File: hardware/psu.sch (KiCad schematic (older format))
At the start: 17 parts

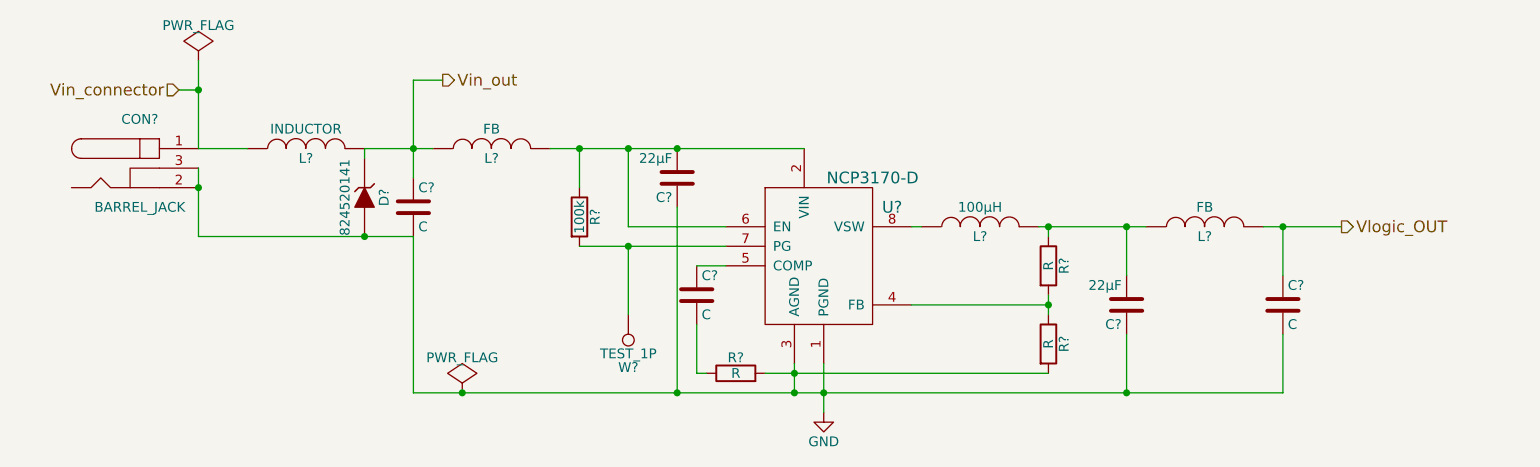
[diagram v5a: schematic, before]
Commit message: Added initial CPU block and fixed bugs from other sheets
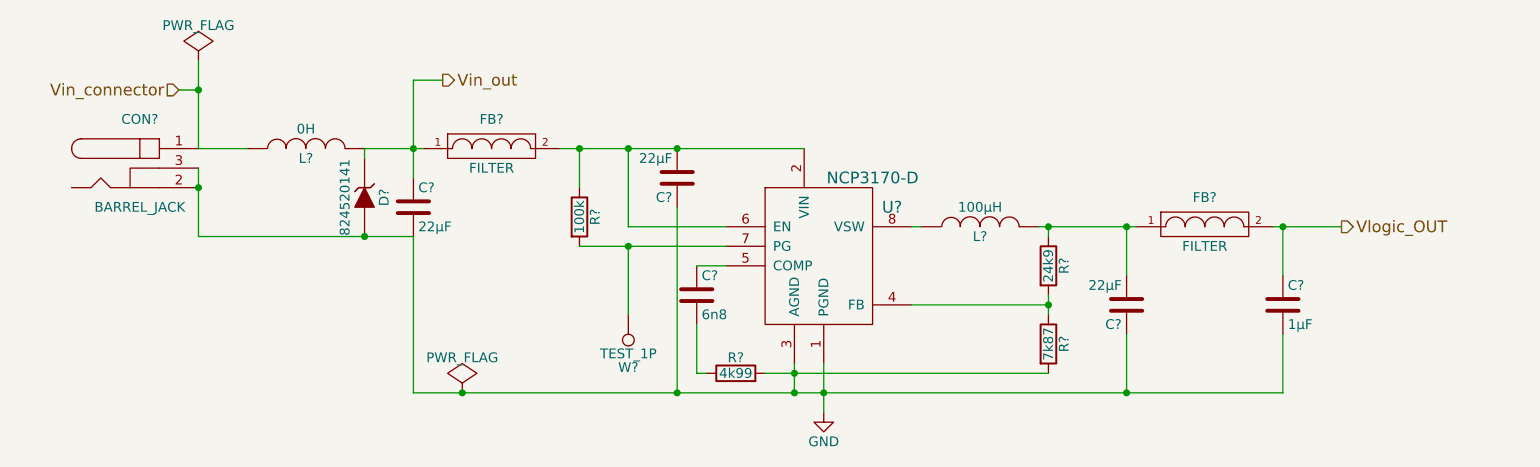
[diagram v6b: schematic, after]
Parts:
- removed L? (x2): FB, symbol INDUCTOR
- added FB? (x2): FILTER, symbol FILTER
- C?: value C -> 6n8
- C?: value C -> 22µF
- C?: value C -> 1µF
- L?: value INDUCTOR -> 0H
- R?: value R -> 24k9
- R?: value R -> 7k87
- R?: value R -> 4k99
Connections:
- net Vin_out: now also FB?.1
- net Vlogic_OUT: now also FB?.2
- net at C?.2, R?.1, U?.2 (VIN)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: now also FB?.2
- net at C?.2, L?.2, R?.1: now also FB?.1
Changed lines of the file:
@@
 LIBS:dodekaedri
 LIBS:Oscillators
+LIBS:stm32
 LIBS:dodekaedri-cache
 EELAYER 25 0
@@
 $Descr A4 11693 8268
 encoding utf-8
-Sheet 4 7
+Sheet 4 8
 Title "Power supply unit"
 Date "2016-09-22"
-Rev "0.1"
+Rev "0.4"
 Comp "PRK - OH2TI"
 Comment1 "exla - OH2EHK"
@@
 P 4800 3700
 F 0 "C?" H 4825 3800 50  0000 L CNN
-F 1 "C" H 4825 3600 50  0000 L CNN
+F 1 "6n8" H 4825 3600 50  0000 L CNN
 F 2 "" H 4838 3550 50  0000 C CNN
 F 3 "" H 4800 3700 50  0000 C CNN
@@
 P 6600 3550
 F 0 "R?" V 6680 3550 50  0000 C CNN
-F 1 "R" V 6600 3550 50  0000 C CNN
+F 1 "24k9" V 6600 3550 50  0000 C CNN
 F 2 "" V 6530 3550 50  0000 C CNN
 F 3 "" H 6600 3550 50  0000 C CNN
@@
 P 6600 3950
 F 0 "R?" V 6680 3950 50  0000 C CNN
-F 1 "R" V 6600 3950 50  0000 C CNN
+F 1 "7k87" V 6600 3950 50  0000 C CNN
 F 2 "" V 6530 3950 50  0000 C CNN
 F 3 "" H 6600 3950 50  0000 C CNN
@@
 P 5000 4100
 F 0 "R?" V 5080 4100 50  0000 C CNN
-F 1 "R" V 5000 4100 50  0000 C CNN
+F 1 "4k99" V 5000 4100 50  0000 C CNN
 F 2 "" V 4930 4100 50  0000 C CNN
 F 3 "" H 5000 4100 50  0000 C CNN
@@
 Wire Wire Line
 	6600 3400 6600 3350
-Wire Wire Line
-	6550 3350 7100 3350
 Wire Wire Line
 	6600 3700 6600 3800
@@
 P 3350 3250
 F 0 "C?" H 3375 3350 50  0000 L CNN
-F 1 "C" H 3375 3150 50  0000 L CNN
+F 1 "22µF" H 3375 3150 50  0000 L CNN
 F 2 "" H 3388 3100 50  0000 C CNN
 F 3 "" H 3350 3250 50  0000 C CNN
@@
 Wire Wire Line
 	2250 3400 3350 3400
-$Comp
-L INDUCTOR L?
-U 1 1 57E32B5E
-P 3750 2950
-F 0 "L?" V 3700 2950 50  0000 C CNN
-F 1 "FB" V 3850 2950 50  0000 C CNN
-F 2 "" H 3750 2950 50  0000 C CNN
-F 3 "" H 3750 2950 50  0000 C CNN
-	1    3750 2950
-	0    -1   -1   0
-$EndComp
-Wire Wire Line
-	4050 2950 5350 2950
+Wire Wire Line
+	4100 2950 5350 2950
 Wire Wire Line
 	4700 3250 4700 4200
 Connection ~ 4700 4200
-$Comp
-L INDUCTOR L?
-U 1 1 57E32E6B
-P 7400 3350
-F 0 "L?" V 7350 3350 50  0000 C CNN
-F 1 "FB" V 7500 3350 50  0000 C CNN
-F 2 "" H 7400 3350 50  0000 C CNN
-F 3 "" H 7400 3350 50  0000 C CNN
-	1    7400 3350
-	0    -1   -1   0
-$EndComp
 $Comp
 L C C?
@@
 P 7800 3750
 F 0 "C?" H 7825 3850 50  0000 L CNN
-F 1 "C" H 7825 3650 50  0000 L CNN
+F 1 "1µF" H 7825 3650 50  0000 L CNN
 F 2 "" H 7838 3600 50  0000 C CNN
 F 3 "" H 7800 3750 50  0000 C CNN
@@
 	1    0    0    -1
 $EndComp
-Wire Wire Line
-	7700 3350 8100 3350
 Connection ~ 7800 3350
 Wire Wire Line
@@
 P 2800 2950
 F 0 "L?" V 2750 2950 50  0000 C CNN
-F 1 "INDUCTOR" V 2900 2950 50  0000 C CNN
+F 1 "0H" V 2900 2950 50  0000 C CNN
 F 2 "" H 2800 2950 50  0000 C CNN
 F 3 "" H 2800 2950 50  0000 C CNN
@@
 $EndComp
 Wire Wire Line
-	3100 2950 3450 2950
+	3100 2950 3400 2950
 Connection ~ 2250 2650
 Wire Wire Line
@@
 Wire Wire Line
 	3500 2600 3350 2600
+$Comp
+L FILTER FB?
+U 1 1 57E5F407
+P 3750 2950
+F 0 "FB?" H 3750 3100 50  0000 C CNN
+F 1 "FILTER" H 3750 2850 50  0000 C CNN
+F 2 "" H 3750 2950 50  0000 C CNN
+F 3 "" H 3750 2950 50  0000 C CNN
+	1    3750 2950
+	1    0    0    -1
+$EndComp
+$Comp
+L FILTER FB?
+U 1 1 57E5F6B8
+P 7400 3350
+F 0 "FB?" H 7400 3500 50  0000 C CNN
+F 1 "FILTER" H 7400 3250 50  0000 C CNN
+F 2 "" H 7400 3350 50  0000 C CNN
+F 3 "" H 7400 3350 50  0000 C CNN
+	1    7400 3350
+	1    0    0    -1
+$EndComp
+Wire Wire Line
+	7750 3350 8100 3350
+Wire Wire Line
+	6550 3350 7050 3350
 $EndSCHEMATC

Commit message: Made some minor adjustments and replotted schematic .pdf
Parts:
- added D?: MSP3V3, symbol ZENER
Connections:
- net GND: now also C?.2, D?.2 (A); no longer C?.1
- net Vlogic_OUT: now also D?.1 (K)
- net at FB?.1, L?.2, R?.1: now also C?.1; no longer C?.2
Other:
- moved on the sheet: C?
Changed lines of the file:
@@
 F 3 "" H 7000 3750 50  0000 C CNN
 	1    7000 3750
-	-1   0    0    1
+	1    0    0    -1
 $EndComp
 $Comp
@@
 	5450 4050 5450 4300
 Wire Wire Line
-	3350 4200 7800 4200
-Wire Wire Line
-	7000 3900 7000 4200
+	3350 4200 8150 4200
 Wire Wire Line
 	7000 3350 7000 3600
@@
 	4950 3350 4450 3350
 Wire Wire Line
-	4450 3350 4450 2950
+	4450 2950 4450 3350
 Connection ~ 4700 2950
 Wire Wire Line
@@
 Connection ~ 4450 2950
 Wire Wire Line
-	2250 3050 2250 3400
+	2250 3050 2250 3450
 Connection ~ 5300 4200
 Connection ~ 2250 3150
@@
 L C C?
 U 1 1 57E32ACD
-P 3350 3250
-F 0 "C?" H 3375 3350 50  0000 L CNN
-F 1 "22µF" H 3375 3150 50  0000 L CNN
-F 2 "" H 3388 3100 50  0000 C CNN
-F 3 "" H 3350 3250 50  0000 C CNN
-	1    3350 3250
-	1    0    0    -1
-$EndComp
-Wire Wire Line
-	2250 3400 3350 3400
+P 3350 3200
+F 0 "C?" H 3375 3300 50  0000 L CNN
+F 1 "22µF" H 3375 3100 50  0000 L CNN
+F 2 "" H 3388 3050 50  0000 C CNN
+F 3 "" H 3350 3200 50  0000 C CNN
+	1    3350 3200
+	1    0    0    -1
+$EndComp
 Wire Wire Line
 	4100 2950 5350 2950
@@
 Wire Wire Line
 	7800 3350 7800 3600
-Text HLabel 8100 3350 2    60   Output ~ 0
+Text HLabel 8350 3350 2    60   Output ~ 0
 Vlogic_OUT
 $Comp
@@
 Connection ~ 2250 2650
 Wire Wire Line
-	3350 2600 3350 3100
+	3350 2600 3350 3050
 $Comp
 L ZENER D?
@@
 	0    1    1    0
 $EndComp
-Connection ~ 3100 3400
-Wire Wire Line
-	3100 3000 3100 2950
+Connection ~ 3100 3450
 Wire Wire Line
 	2250 2950 2500 2950
 Wire Wire Line
-	3350 3400 3350 4200
+	3350 3350 3350 4200
 Text HLabel 3500 2600 2    60   Output ~ 0
 Vin_out
@@
 $EndComp
 Wire Wire Line
-	7750 3350 8100 3350
+	7750 3350 8350 3350
 Wire Wire Line
 	6550 3350 7050 3350
+$Comp
+L ZENER D?
+U 1 1 57ED7CD8
+P 8150 3750
+F 0 "D?" H 8150 3850 50  0000 C CNN
+F 1 "MSP3V3" H 8150 3650 50  0000 C CNN
+F 2 "" H 8150 3750 50  0000 C CNN
+F 3 "" H 8150 3750 50  0000 C CNN
+	1    8150 3750
+	0    1    1    0
+$EndComp
+Wire Wire Line
+	8150 3550 8150 3350
+Connection ~ 8150 3350
+Wire Wire Line
+	8150 4200 8150 3950
+Connection ~ 7800 4200
+Connection ~ 3350 3450
+Wire Wire Line
+	3100 3000 3100 2950
+Wire Wire Line
+	2250 3450 3350 3450
+Wire Wire Line
+	3100 3400 3100 3450
+Wire Wire Line
+	7000 3900 7000 4200
 $EndSCHEMATC

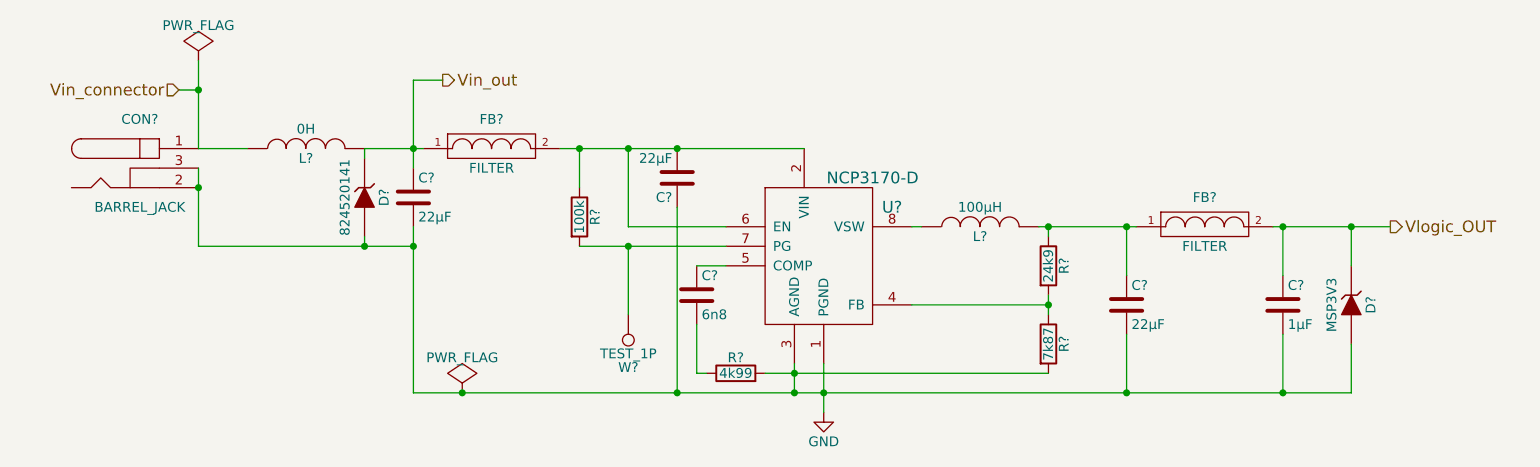
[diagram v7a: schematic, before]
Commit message: Fixed 8/11 of issue #4
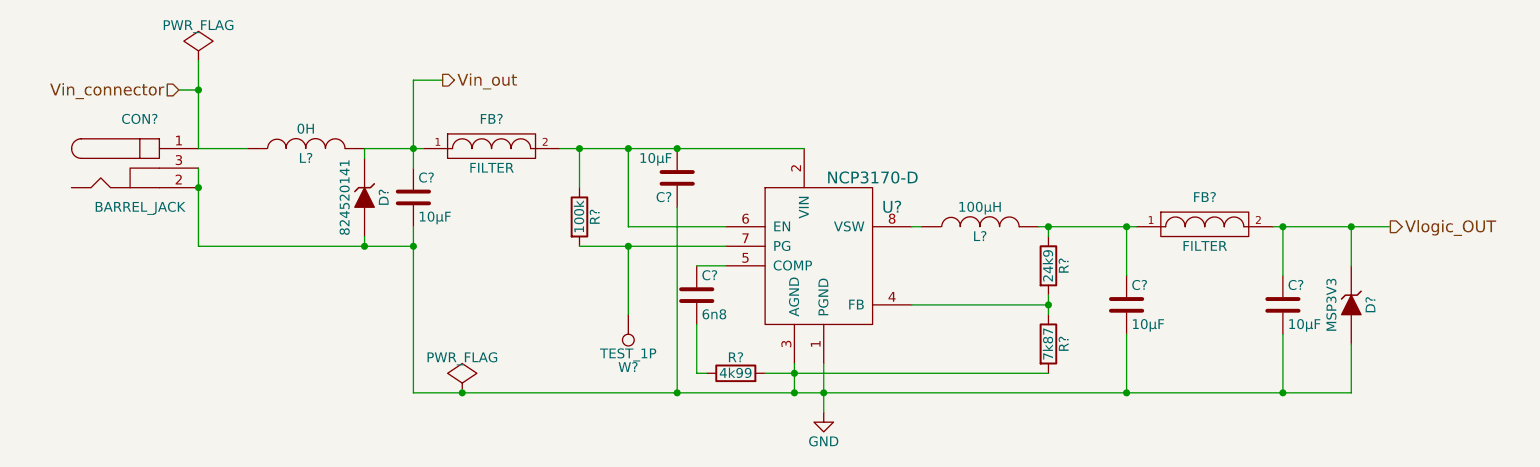
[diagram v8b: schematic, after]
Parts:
- C? (x3): value 22µF -> 10µF
- C?: value 1µF -> 10µF
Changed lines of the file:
@@
 P 4700 3100
 F 0 "C?" H 4725 3200 50  0000 L CNN
-F 1 "22µF" H 4725 3000 50  0000 L CNN
+F 1 "10µF" H 4725 3000 50  0000 L CNN
 F 2 "" H 4738 2950 50  0000 C CNN
 F 3 "" H 4700 3100 50  0000 C CNN
@@
 P 7000 3750
 F 0 "C?" H 7025 3850 50  0000 L CNN
-F 1 "22µF" H 7025 3650 50  0000 L CNN
+F 1 "10µF" H 7025 3650 50  0000 L CNN
 F 2 "" H 7038 3600 50  0000 C CNN
 F 3 "" H 7000 3750 50  0000 C CNN
@@
 	4950 3350 4450 3350
 Wire Wire Line
-	4450 2950 4450 3350
+	4450 3350 4450 2950
 Connection ~ 4700 2950
 Wire Wire Line
@@
 P 3350 3200
 F 0 "C?" H 3375 3300 50  0000 L CNN
-F 1 "22µF" H 3375 3100 50  0000 L CNN
+F 1 "10µF" H 3375 3100 50  0000 L CNN
 F 2 "" H 3388 3050 50  0000 C CNN
 F 3 "" H 3350 3200 50  0000 C CNN
@@
 P 7800 3750
 F 0 "C?" H 7825 3850 50  0000 L CNN
-F 1 "1µF" H 7825 3650 50  0000 L CNN
+F 1 "10µF" H 7825 3650 50  0000 L CNN
 F 2 "" H 7838 3600 50  0000 C CNN
 F 3 "" H 7800 3750 50  0000 C CNN
